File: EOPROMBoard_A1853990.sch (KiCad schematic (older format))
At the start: 0 parts

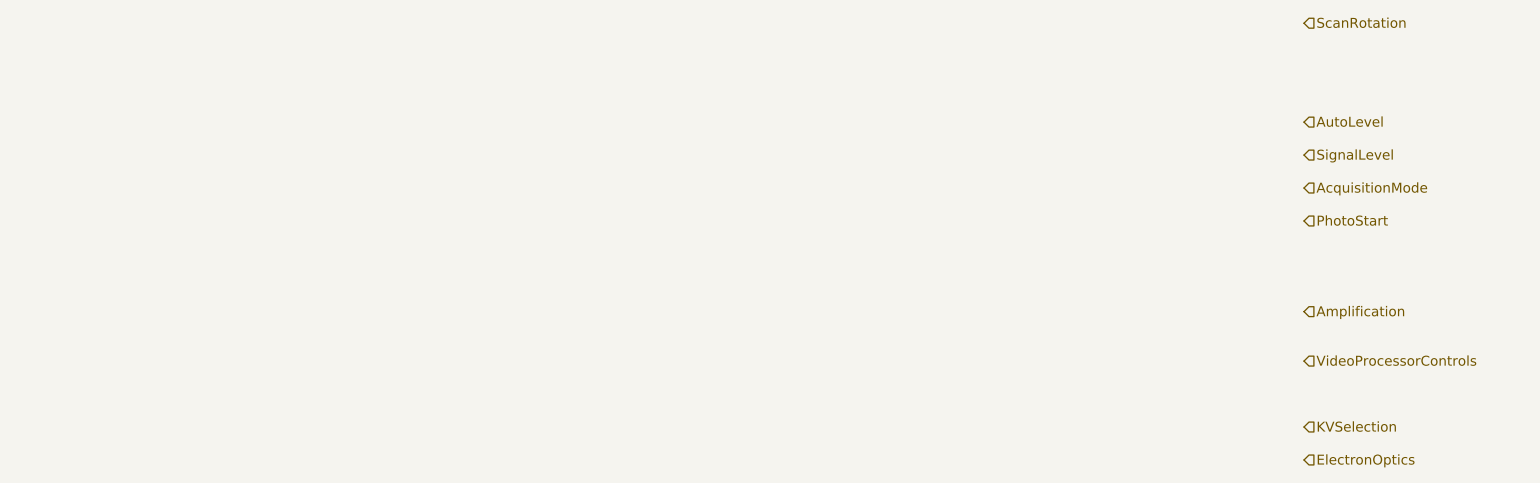
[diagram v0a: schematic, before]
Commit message: Adds EOProm Board PCB
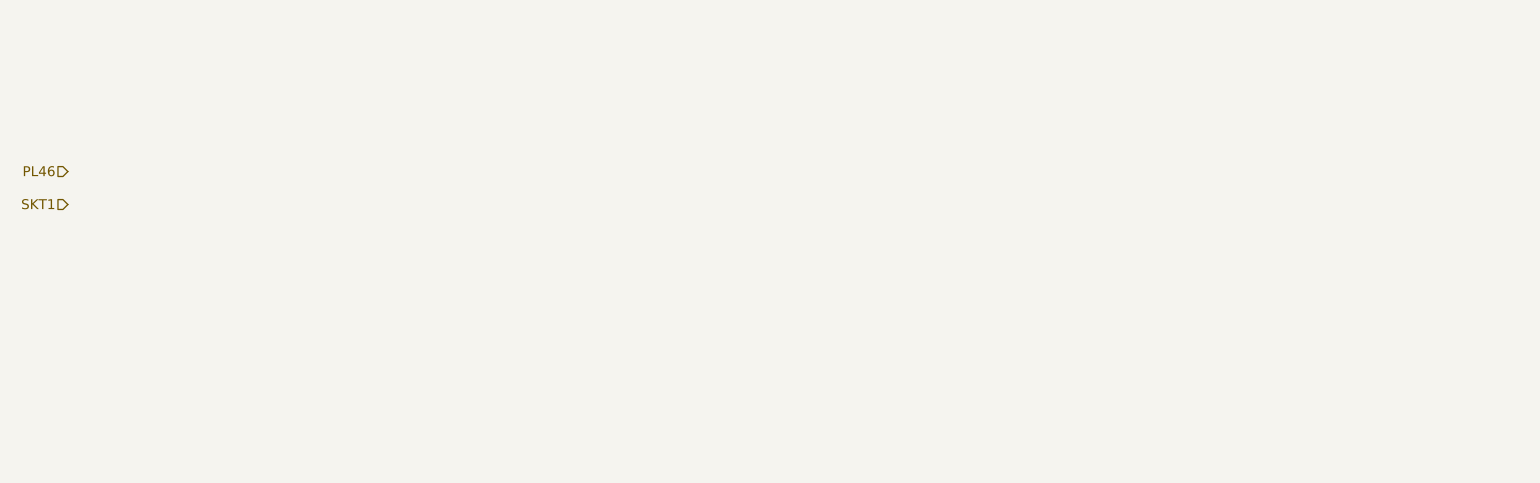
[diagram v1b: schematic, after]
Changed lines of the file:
@@
 $Descr A4 11693 8268
 encoding utf-8
-Sheet 12 18
+Sheet 18 18
 Title ""
 Date ""
@@
 Comment4 ""
 $EndDescr
-Text HLabel 9550 1000 2    60   Input ~ 0
-ScanRotation
-Text HLabel 9550 1600 2    60   Input ~ 0
-AutoLevel
-Text HLabel 9550 1800 2    60   Input ~ 0
-SignalLevel
-Text HLabel 9550 2000 2    60   Input ~ 0
-AcquisitionMode
-Text HLabel 9550 2200 2    60   Input ~ 0
-PhotoStart
-Text HLabel 9550 2750 2    60   Input ~ 0
-Amplification
-Text HLabel 9550 3050 2    60   Input ~ 0
-VideoProcessorControls
-Text HLabel 9550 3450 2    60   Input ~ 0
-KVSelection
-Text HLabel 9550 3650 2    60   Input ~ 0
-ElectronOptics
+Text HLabel 2050 2100 0    60   Input ~ 0
+SKT1
+Text HLabel 2050 1900 0    60   Input ~ 0
+PL46
 $EndSCHEMATC
